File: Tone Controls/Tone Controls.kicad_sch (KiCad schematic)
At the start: 53 parts, among them J1 Barrel_Jack, J2 Barrel_Jack, Q1 2N3904, Q2 2N3904, SW2 DSP_EN, SW3 Chorus_EN, U3 TL072, U4 TL072

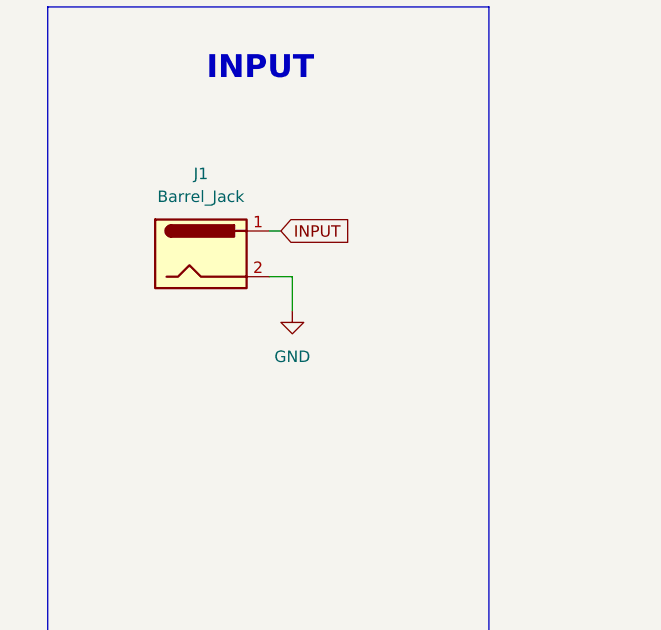
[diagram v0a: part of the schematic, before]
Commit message: add block diagram
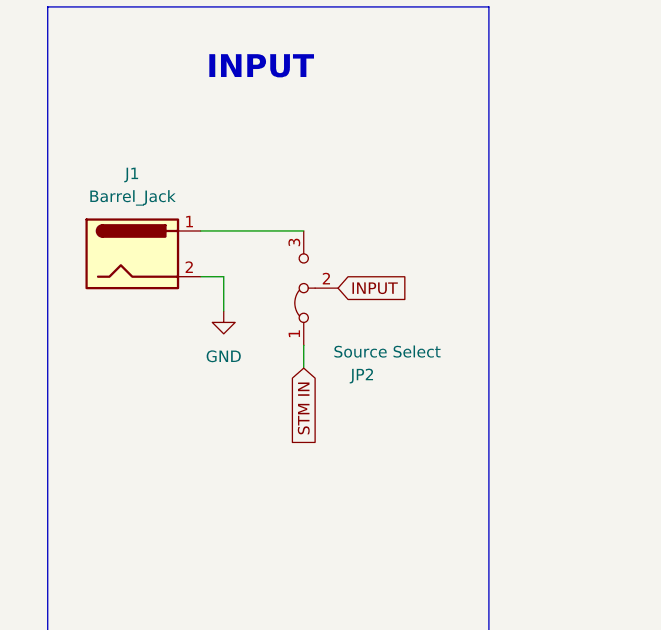
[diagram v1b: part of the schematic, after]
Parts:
- added JP2: Source Select, symbol Jumper:Jumper_3_Bridged12
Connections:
- net INPUT: now also JP2.2 (C); no longer J1.1
- new net: J1.1, JP2.3 (B)
- new net STM IN: JP2.1 (A)
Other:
- moved on the sheet: J1
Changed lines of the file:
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@@
 	(wire
 		(pts
+			(xy 49.53 208.28) (xy 49.53 205.74)
+		)
+		(stroke
+			(width 0)
+			(type default)
+		)
+	)
+	(wire
+		(pts
 			(xy 247.65 95.25) (xy 247.65 92.71)
 		)
@@
 	(wire
 		(pts
-			(xy 48.26 198.12) (xy 45.72 198.12)
+			(xy 40.64 198.12) (xy 38.1 198.12)
 		)
 		(stroke
@@
 	(wire
 		(pts
-			(xy 48.26 201.93) (xy 48.26 198.12)
+			(xy 40.64 201.93) (xy 40.64 198.12)
 		)
 		(stroke
@@
 	(wire
 		(pts
-			(xy 46.99 193.04) (xy 45.72 193.04)
+			(xy 38.1 193.04) (xy 49.53 193.04)
 		)
 		(stroke
@@
 	(global_label "INPUT"
 		(shape input)
-		(at 46.99 193.04 0)
+		(at 53.34 199.39 0)
 		(fields_autoplaced yes)
 		(effects
@@
 		)
 		(property "Intersheetrefs" "${INTERSHEET_REFS}"
-			(at 55.4786 193.04 0)
+			(at 61.8286 199.39 0)
 			(effects
 				(font
@@
 		)
 	)
+	(global_label "STM IN"
+		(shape input)
+		(at 49.53 208.28 270)
+		(fields_autoplaced yes)
+		(effects
+			(font
+				(size 1.27 1.27)
+			)
+			(justify right)
+		)
+		(property "Intersheetrefs" "${INTERSHEET_REFS}"
+			(at 49.53 217.7966 90)
+			(effects
+				(font
+					(size 1.27 1.27)
+				)
+				(justify right)
+				(hide yes)
+			)
+		)
+	)
 	(global_label "Signal_OUT"
 		(shape input)
@@
 	(symbol
 		(lib_id "power:GND")
-		(at 48.26 201.93 0)
+		(at 40.64 201.93 0)
 		(unit 1)
 		(exclude_from_sim no)
@@
 		(fields_autoplaced yes)
 		(property "Reference" "#PWR07"
-			(at 48.26 208.28 0)
+			(at 40.64 208.28 0)
 			(effects
 				(font
@@
 		)
 		(property "Value" "GND"
-			(at 48.26 207.01 0)
+			(at 40.64 207.01 0)
 			(effects
 				(font
@@
 		)
 		(property "Footprint" ""
-			(at 48.26 201.93 0)
+			(at 40.64 201.93 0)
 			(effects
 				(font
@@
 		)
 		(property "Datasheet" ""
-			(at 48.26 201.93 0)
+			(at 40.64 201.93 0)
 			(effects
 				(font
@@
 		)
 		(property "Description" "Power symbol creates a global label with name \"GND\" , ground"
-			(at 48.26 201.93 0)
+			(at 40.64 201.93 0)
 			(effects
 				(font
@@
 	)
 	(symbol
+		(lib_id "Jumper:Jumper_3_Bridged12")
+		(at 49.53 199.39 90)
+		(unit 1)
+		(exclude_from_sim yes)
+		(in_bom no)
+		(on_board yes)
+		(dnp no)
+		(property "Reference" "JP2"
+			(at 57.404 209.042 90)
+			(effects
+				(font
+					(size 1.27 1.27)
+				)
+				(justify left)
+			)
+		)
+		(property "Value" "Source Select"
+			(at 64.77 206.502 90)
+			(effects
+				(font
+					(size 1.27 1.27)
+				)
+				(justify left)
+			)
+		)
+		(property "Footprint" ""
+			(at 49.53 199.39 0)
+			(effects
+				(font
+					(size 1.27 1.27)
+				)
+				(hide yes)
+			)
+		)
+		(property "Datasheet" "~"
+			(at 49.53 199.39 0)
+			(effects
+				(font
+					(size 1.27 1.27)
+				)
+				(hide yes)
+			)
+		)
+		(property "Description" "Jumper, 3-pole, pins 1+2 closed/bridged"
+			(at 49.53 199.39 0)
+			(effects
+				(font
+					(size 1.27 1.27)
+				)
+				(hide yes)
+			)
+		)
+		(pin "3"
+		)
+		(pin "2"
+		)
+		(pin "1"
+		)
+		(instances
+			(project "Tone Controls"
+				(path "/3897f13b-fd60-416d-8efd-dedd3c4d72d9"
+					(reference "JP2")
+					(unit 1)
+				)
+			)
+		)
+	)
+	(symbol
 		(lib_id "Device:R_Potentiometer")
 		(at 165.1 81.28 90)
@@
 	(symbol
 		(lib_id "Connector:Barrel_Jack")
-		(at 38.1 195.58 0)
+		(at 30.48 195.58 0)
 		(unit 1)
 		(exclude_from_sim no)
@@
 		(fields_autoplaced yes)
 		(property "Reference" "J1"
-			(at 38.1 186.69 0)
+			(at 30.48 186.69 0)
 			(effects
 				(font
@@
 		)
 		(property "Value" "Barrel_Jack"
-			(at 38.1 189.23 0)
+			(at 30.48 189.23 0)
 			(effects
 				(font
@@
 		)
 		(property "Footprint" "Connector_BarrelJack:BarrelJack_SwitchcraftConxall_RAPC10U_Horizontal"
-			(at 39.37 196.596 0)
+			(at 31.75 196.596 0)
 			(effects
 				(font
@@
 		)
 		(property "Datasheet" "~"
-			(at 39.37 196.596 0)
+			(at 31.75 196.596 0)
 			(effects
 				(font
@@
 		)
 		(property "Description" "DC Barrel Jack"
-			(at 38.1 195.58 0)
+			(at 30.48 195.58 0)
 			(effects
 				(font

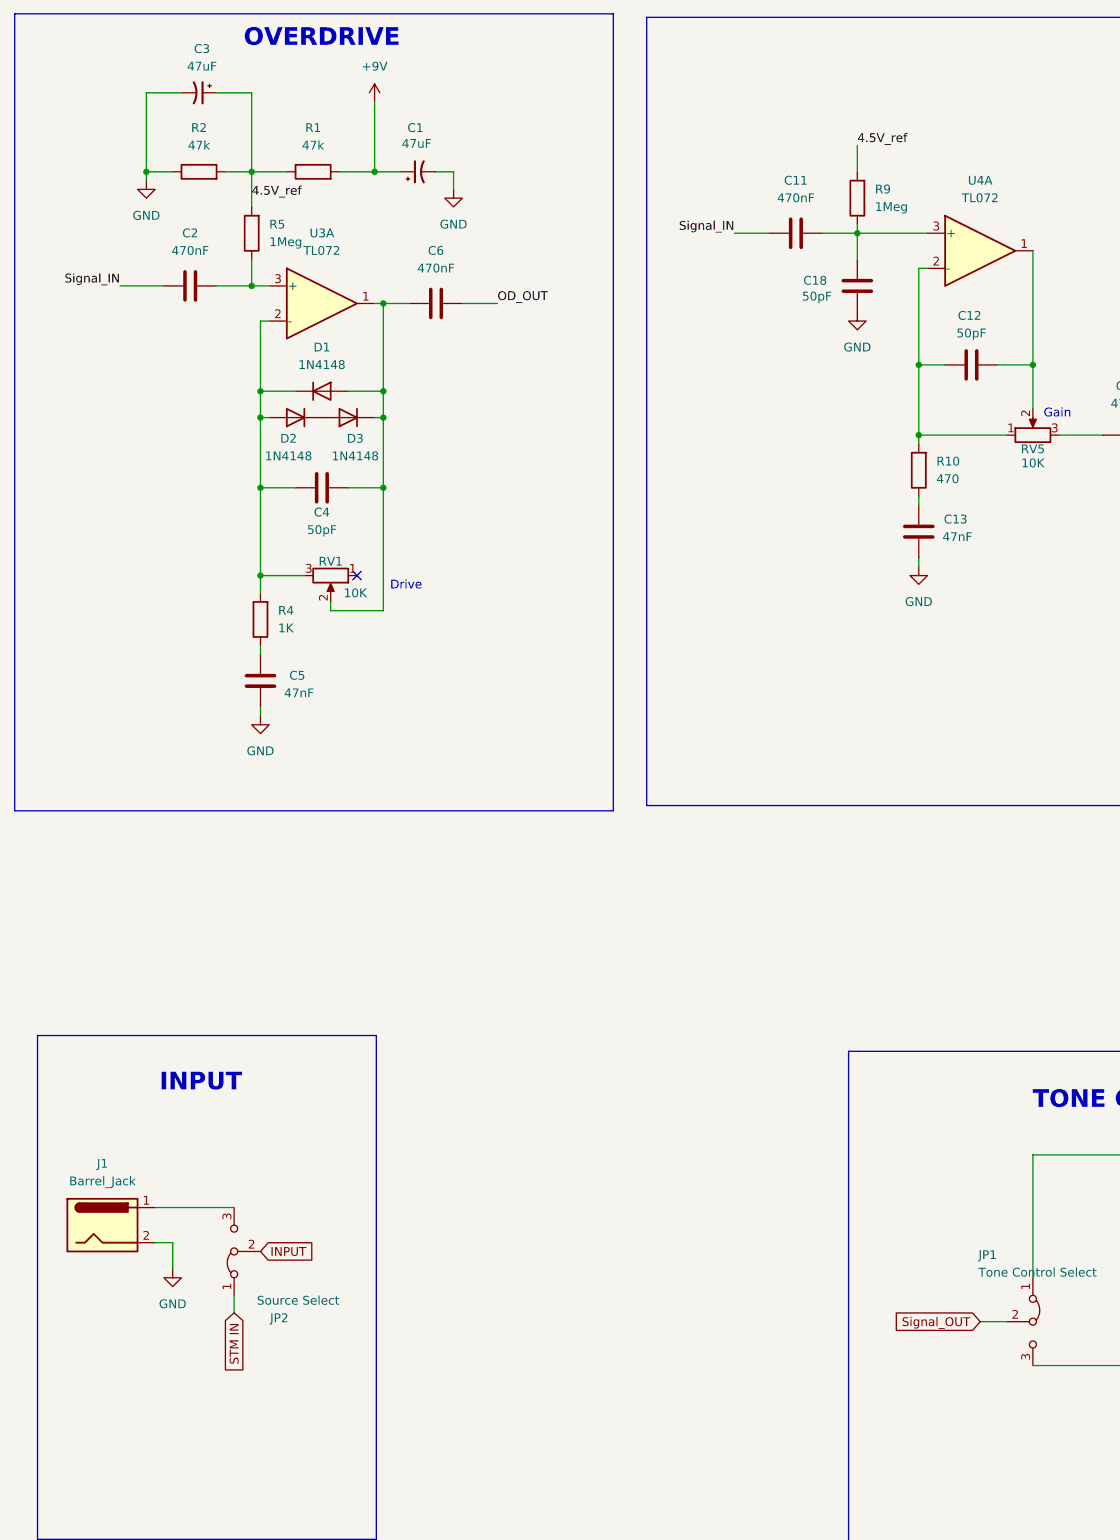
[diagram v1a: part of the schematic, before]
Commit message: add BOM
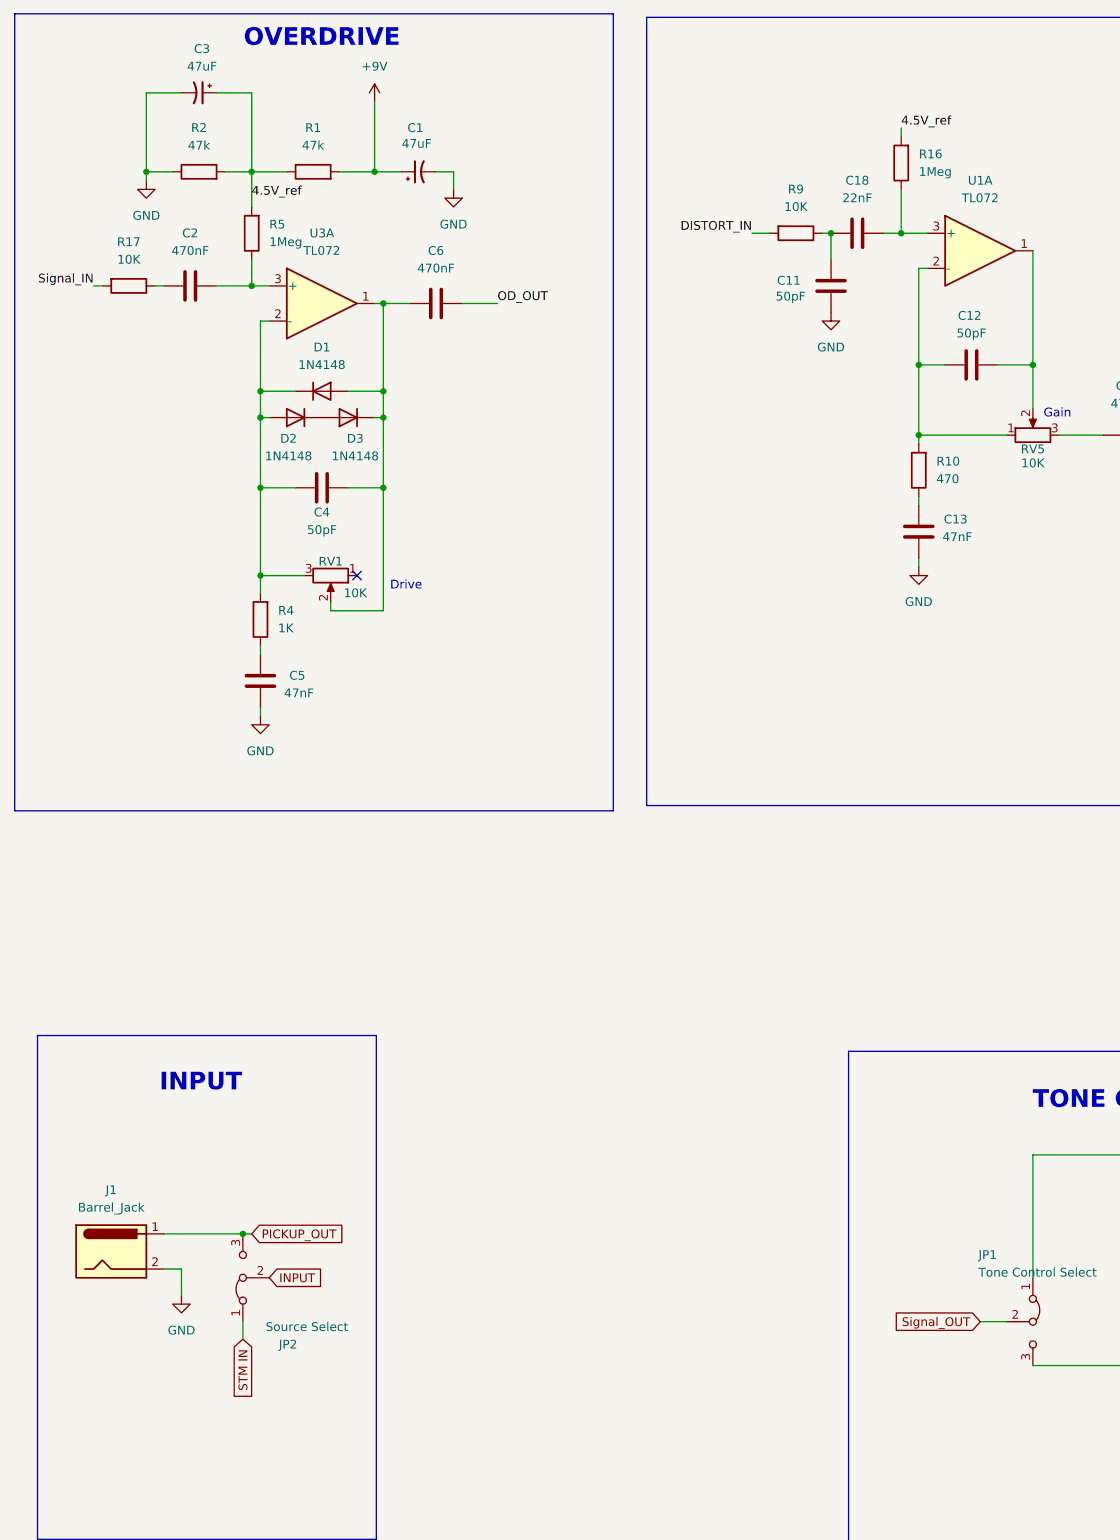
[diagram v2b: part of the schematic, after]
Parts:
- removed unit 1 of U4
- added R16: 1Meg, Resistor_SMD:R_0805_2012Metric_Pad1.20x1.40mm_HandSolder, symbol Device:R
- added R17: 10K, Resistor_SMD:R_0805_2012Metric_Pad1.20x1.40mm_HandSolder, symbol Device:R
- added U1: TL072, symbol Amplifier_Operational:TL072
- C11: value 470nF -> 50pF
- C18: value 50pF -> 22nF
- R9: value 1Meg -> 10K
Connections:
- net 4.5V_ref: now also R16.2; no longer R9.2
- net GND: now also C11.2; no longer C18.2
- net Signal_IN: now also R17.2; no longer C11.1, C2.1
- net at C12.1, RV5.2: now also U1.1
- net at C12.2, R10.2, RV5.1: now also U1.2 (-)
- net at C18.1, R9.1: now also C11.1; no longer C11.2
- net PICKUP_OUT: now reaches J1.1, JP2.3 (B)
- new net: C2.1, R17.1
- new net: C18.2, R16.1, U1.3 (+)
- new net DISTORT_IN: R9.2

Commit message: R2
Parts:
- removed unit 2 of U3
- RV1, RV4, RV5: value 10K -> 100K
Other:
- moved on the sheet: C10, C11, C12, C13, C14, C15, C16, C17, C18, C8, C9, D4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

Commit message: V1.0
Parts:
- removed JP1: Tone Control Select, symbol Jumper:Jumper_3_Bridged12
- R11: value 4.7K -> 10k
- R12: value 330K -> 680K
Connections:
- net Signal_OUT: now also C7.2, R14.2
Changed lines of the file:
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@@
 	)
 	(junction
-		(at 215.9 215.9)
-		(diameter 0)
-		(color 0 0 0 0)
-	)
-	(junction
 		(at 240.03 78.74)
 		(diameter 0)
@@
 	(wire
 		(pts
-			(xy 165.1 185.42) (xy 165.1 203.2)
-		)
-		(stroke
-			(width 0)
-			(type default)
-		)
-	)
-	(wire
-		(pts
 			(xy 52.07 43.18) (xy 57.15 43.18)
 		)
@@
 	(wire
 		(pts
-			(xy 165.1 215.9) (xy 180.34 215.9)
-		)
-		(stroke
-			(width 0)
-			(type default)
-		)
-	)
-	(wire
-		(pts
 			(xy 71.12 88.9) (xy 71.12 106.68)
 		)
@@
 	(wire
 		(pts
-			(xy 165.1 185.42) (xy 215.9 185.42)
-		)
-		(stroke
-			(width 0)
-			(type default)
-		)
-	)
-	(wire
-		(pts
 			(xy 345.44 45.72) (xy 337.82 45.72)
 		)
@@
 	(wire
 		(pts
-			(xy 215.9 185.42) (xy 215.9 215.9)
-		)
-		(stroke
-			(width 0)
-			(type default)
-		)
-	)
-	(wire
-		(pts
 			(xy 53.34 64.77) (xy 53.34 74.93)
 		)
@@
 	(wire
 		(pts
-			(xy 157.48 209.55) (xy 161.29 209.55)
+			(xy 165.1 215.9) (xy 180.34 215.9)
 		)
 		(stroke
@@
 	(global_label "Signal_OUT"
 		(shape input)
-		(at 157.48 209.55 180)
+		(at 165.1 215.9 180)
 		(fields_autoplaced yes)
 		(effects
@@
 		)
 		(property "Intersheetrefs" "${INTERSHEET_REFS}"
-			(at 143.9721 209.55 0)
+			(at 151.5921 215.9 0)
 			(effects
 				(font
@@
 			)
 		)
-		(property "Value" "4.7K"
+		(property "Value" "10k"
 			(at 186.69 77.47 90)
 			(effects
@@
 	)
 	(symbol
-		(lib_id "Jumper:Jumper_3_Bridged12")
-		(at 165.1 209.55 270)
-		(unit 1)
-		(exclude_from_sim no)
-		(in_bom no)
-		(on_board yes)
-		(dnp no)
-		(property "Reference" "JP1"
-			(at 157.226 199.898 90)
-			(effects
-				(font
-					(size 1.27 1.27)
-				)
-				(justify left)
-			)
-		)
-		(property "Value" "Tone Control Select"
-			(at 157.226 202.438 90)
-			(effects
-				(font
-					(size 1.27 1.27)
-				)
-				(justify left)
-			)
-		)
-		(property "Footprint" ""
-			(at 165.1 209.55 0)
-			(effects
-				(font
-					(size 1.27 1.27)
-				)
-				(hide yes)
-			)
-		)
-		(property "Datasheet" "~"
-			(at 165.1 209.55 0)
-			(effects
-				(font
-					(size 1.27 1.27)
-				)
-				(hide yes)
-			)
-		)
-		(property "Description" "Jumper, 3-pole, pins 1+2 closed/bridged"
-			(at 165.1 209.55 0)
-			(effects
-				(font
-					(size 1.27 1.27)
-				)
-				(hide yes)
-			)
-		)
-		(pin "3"
-		)
-		(pin "2"
-		)
-		(pin "1"
-		)
-		(instances
-			(project "Tone Controls"
-				(path "/3897f13b-fd60-416d-8efd-dedd3c4d72d9"
-					(reference "JP1")
-					(unit 1)
-				)
-			)
-		)
-	)
-	(symbol
 		(lib_id "power:+9V")
 		(at 69.85 33.02 0)
@@
 			)
 		)
-		(property "Value" "330K"
+		(property "Value" "680K"
 			(at 208.28 102.87 90)
 			(effects

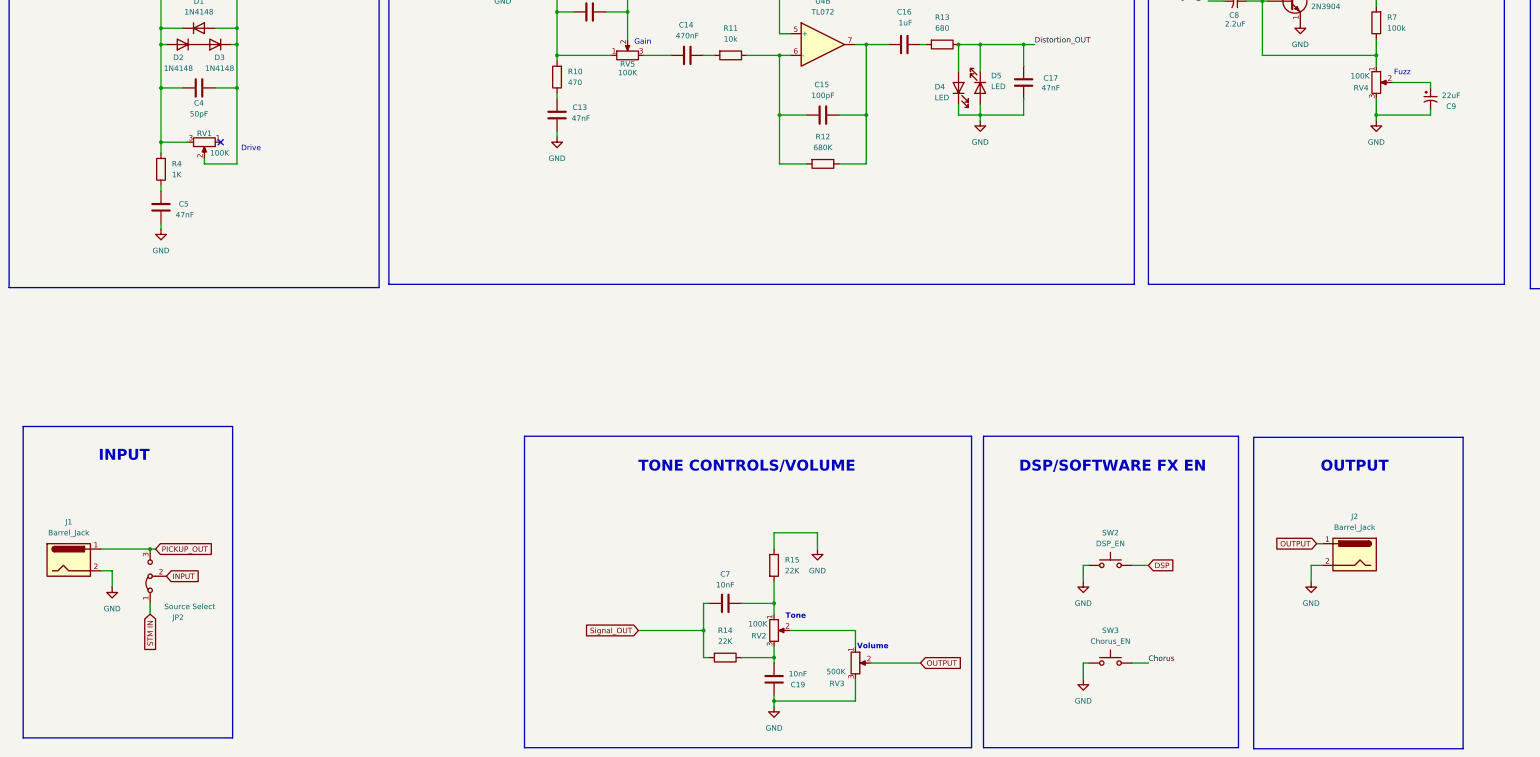
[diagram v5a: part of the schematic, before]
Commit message: Replace pdf with project circuit version
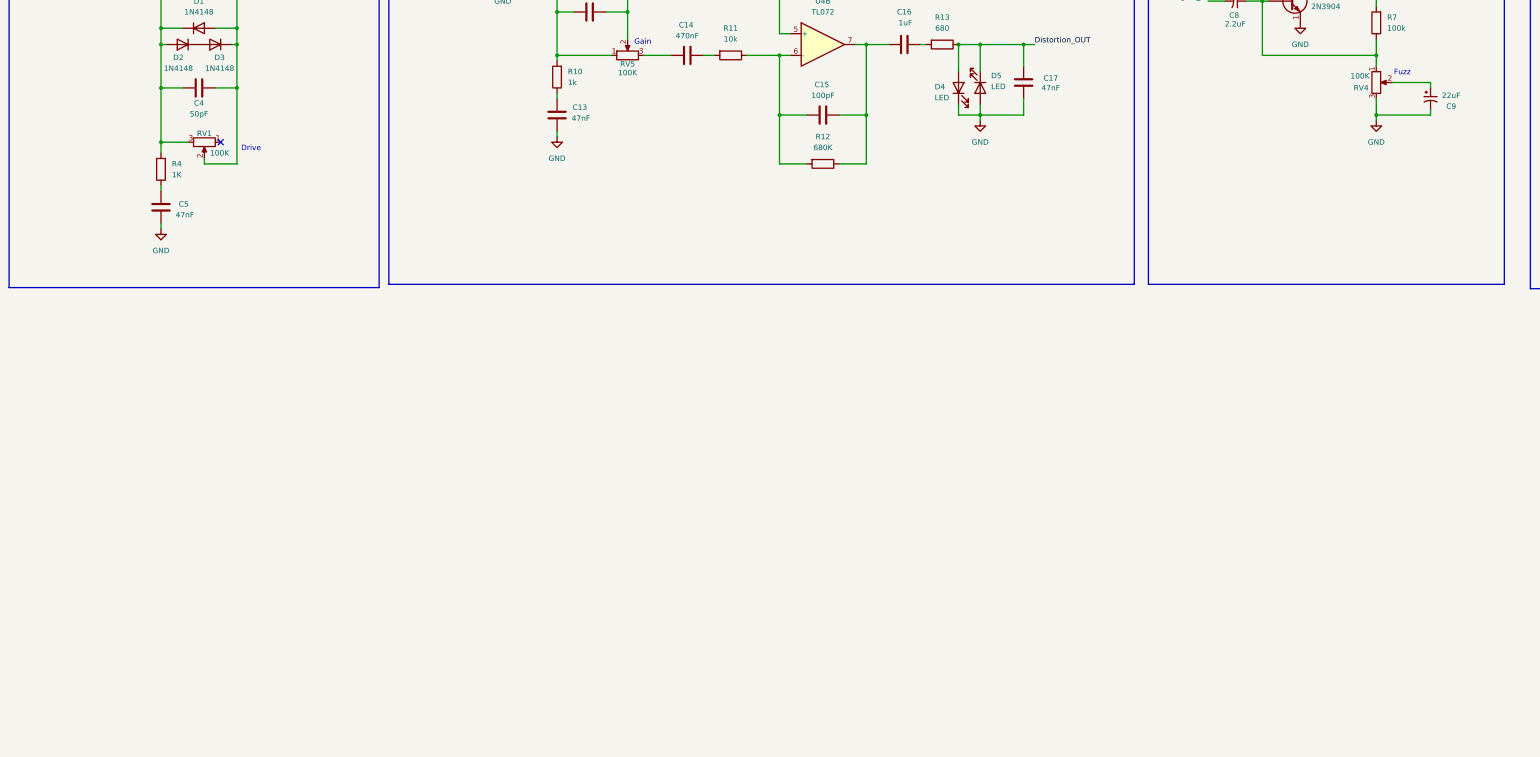
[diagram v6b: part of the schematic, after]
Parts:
- removed C19, C7: 10nF, Capacitor_THT:C_Disc_D3.8mm_W2.6mm_P2.50mm, symbol Device:C
- removed J1, J2: Barrel_Jack, Connector_BarrelJack:BarrelJack_SwitchcraftConxall_RAPC10U_Horizontal, symbol Connector:Barrel_Jack
- removed JP2: Source Select, symbol Jumper:Jumper_3_Bridged12
- removed R14, R15: 22K, Resistor_SMD:R_0805_2012Metric_Pad1.20x1.40mm_HandSolder, symbol Device:R
- removed RV2: 100K, Potentiometer_THT:Potentiometer_Piher_PT-15-V02_Vertical, symbol Device:R_Potentiometer
- removed RV3: 500K, Potentiometer_THT:Potentiometer_Piher_PT-15-V02_Vertical, symbol Device:R_Potentiometer
- removed SW2: DSP_EN, symbol Switch:SW_Push
- removed SW3: Chorus_EN, symbol Switch:SW_Push
- R10: value 470 -> 1k
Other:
- note removed: "DSP/SOFTWARE FX EN"
- note removed: "INPUT"
- note removed: "OUTPUT"
- note removed: "TONE CONTROLS/VOLUME"
- note removed: "Tone"
- note removed: "Volume"
